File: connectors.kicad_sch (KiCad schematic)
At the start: 4 parts, among them J1 Conn_01x04_Male, J2 Conn_01x04_Male, J3 Conn_01x09_Male, J4 Conn_02x03_Odd_Even

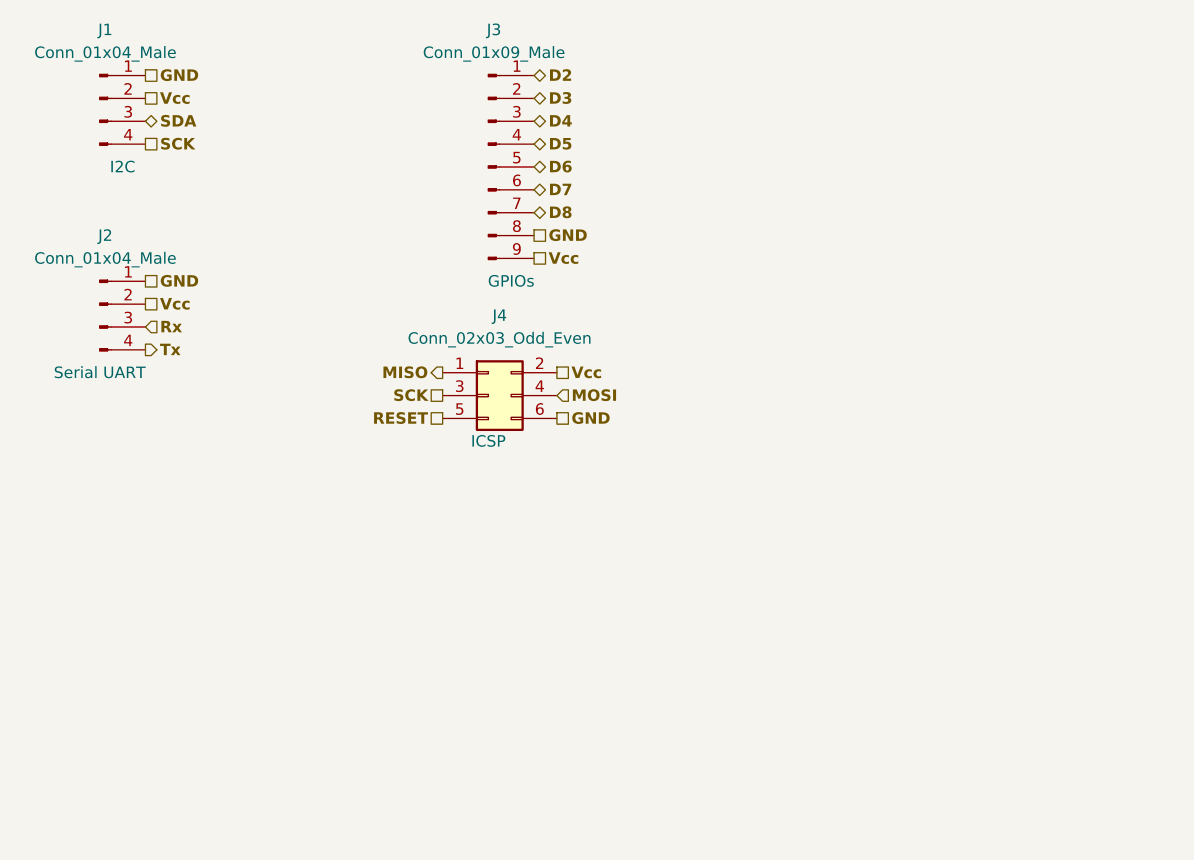
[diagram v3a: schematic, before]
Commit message: Routing GND Vcc completed
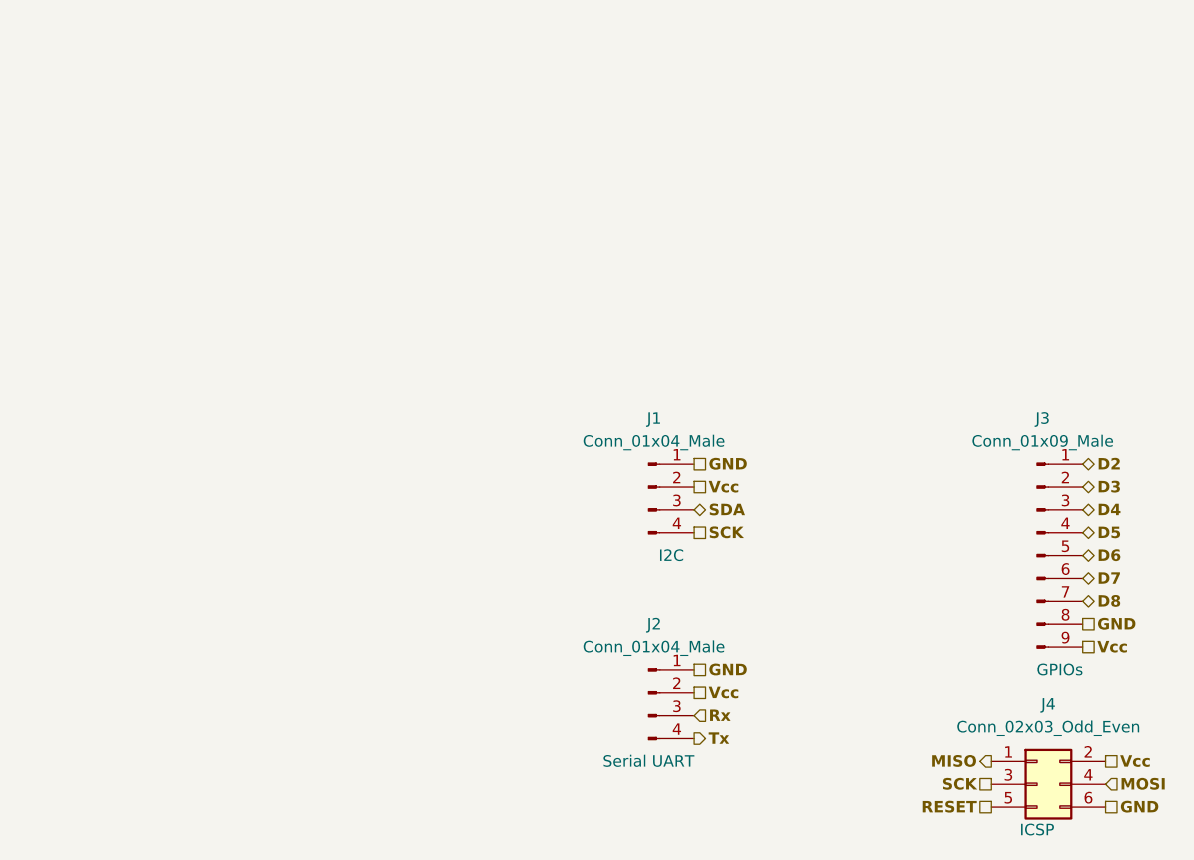
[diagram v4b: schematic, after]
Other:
- moved on the sheet: J1, J2, J3, J4
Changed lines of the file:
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@@
 (kicad_sch (version 20211123) (generator eeschema)
   (paper "A4")
-  (hierarchical_label "GND" (shape passive) (at 109.22 50.8 0)
+  (hierarchical_label "GND" (shape passive) (at 170.18 93.98 0)
     (effects (font (size 1.27 1.27) bold) (justify left))
   )
-  (hierarchical_label "D6" (shape bidirectional) (at 109.22 43.18 0)
+  (hierarchical_label "D6" (shape bidirectional) (at 170.18 86.36 0)
     (effects (font (size 1.27 1.27) bold) (justify left))
   )
-  (hierarchical_label "SCK" (shape passive) (at 66.04 40.64 0)
+  (hierarchical_label "SCK" (shape passive) (at 127 83.82 0)
     (effects (font (size 1.27 1.27) bold) (justify left))
   )
-  (hierarchical_label "D3" (shape bidirectional) (at 109.22 35.56 0)
+  (hierarchical_label "D3" (shape bidirectional) (at 170.18 78.74 0)
     (effects (font (size 1.27 1.27) bold) (justify left))
   )
-  (hierarchical_label "Rx" (shape input) (at 66.04 60.96 0)
+  (hierarchical_label "Rx" (shape input) (at 127 104.14 0)
     (effects (font (size 1.27 1.27) bold) (justify left))
   )
-  (hierarchical_label "RESET" (shape passive) (at 99.06 71.12 180)
+  (hierarchical_label "RESET" (shape passive) (at 160.02 114.3 180)
     (effects (font (size 1.27 1.27) bold) (justify right))
   )
-  (hierarchical_label "D7" (shape bidirectional) (at 109.22 45.72 0)
+  (hierarchical_label "D7" (shape bidirectional) (at 170.18 88.9 0)
     (effects (font (size 1.27 1.27) bold) (justify left))
   )
-  (hierarchical_label "Tx" (shape output) (at 66.04 63.5 0)
+  (hierarchical_label "Tx" (shape output) (at 127 106.68 0)
     (effects (font (size 1.27 1.27) bold) (justify left))
   )
-  (hierarchical_label "SCK" (shape passive) (at 99.06 68.58 180)
+  (hierarchical_label "SCK" (shape passive) (at 160.02 111.76 180)
     (effects (font (size 1.27 1.27) bold) (justify right))
   )
-  (hierarchical_label "Vcc" (shape passive) (at 66.04 58.42 0)
+  (hierarchical_label "Vcc" (shape passive) (at 127 101.6 0)
     (effects (font (size 1.27 1.27) bold) (justify left))
   )
-  (hierarchical_label "D4" (shape bidirectional) (at 109.22 38.1 0)
+  (hierarchical_label "D4" (shape bidirectional) (at 170.18 81.28 0)
     (effects (font (size 1.27 1.27) bold) (justify left))
   )
-  (hierarchical_label "D2" (shape bidirectional) (at 109.22 33.02 0)
+  (hierarchical_label "D2" (shape bidirectional) (at 170.18 76.2 0)
     (effects (font (size 1.27 1.27) bold) (justify left))
   )
-  (hierarchical_label "GND" (shape passive) (at 66.04 55.88 0)
+  (hierarchical_label "GND" (shape passive) (at 127 99.06 0)
     (effects (font (size 1.27 1.27) bold) (justify left))
   )
-  (hierarchical_label "Vcc" (shape passive) (at 66.04 35.56 0)
+  (hierarchical_label "Vcc" (shape passive) (at 127 78.74 0)
     (effects (font (size 1.27 1.27) bold) (justify left))
   )
-  (hierarchical_label "SDA" (shape bidirectional) (at 66.04 38.1 0)
+  (hierarchical_label "SDA" (shape bidirectional) (at 127 81.28 0)
     (effects (font (size 1.27 1.27) bold) (justify left))
   )
-  (hierarchical_label "GND" (shape passive) (at 66.04 33.02 0)
+  (hierarchical_label "GND" (shape passive) (at 127 76.2 0)
     (effects (font (size 1.27 1.27) bold) (justify left))
   )
-  (hierarchical_label "D8" (shape bidirectional) (at 109.22 48.26 0)
+  (hierarchical_label "D8" (shape bidirectional) (at 170.18 91.44 0)
     (effects (font (size 1.27 1.27) bold) (justify left))
   )
-  (hierarchical_label "Vcc" (shape passive) (at 109.22 53.34 0)
+  (hierarchical_label "Vcc" (shape passive) (at 170.18 96.52 0)
     (effects (font (size 1.27 1.27) bold) (justify left))
   )
-  (hierarchical_label "MOSI" (shape input) (at 111.76 68.58 0)
+  (hierarchical_label "MOSI" (shape input) (at 172.72 111.76 0)
     (effects (font (size 1.27 1.27) bold) (justify left))
   )
-  (hierarchical_label "Vcc" (shape passive) (at 111.76 66.04 0)
+  (hierarchical_label "Vcc" (shape passive) (at 172.72 109.22 0)
     (effects (font (size 1.27 1.27) bold) (justify left))
   )
-  (hierarchical_label "D5" (shape bidirectional) (at 109.22 40.64 0)
+  (hierarchical_label "D5" (shape bidirectional) (at 170.18 83.82 0)
     (effects (font (size 1.27 1.27) bold) (justify left))
   )
-  (hierarchical_label "MISO" (shape output) (at 99.06 66.04 180)
+  (hierarchical_label "MISO" (shape output) (at 160.02 109.22 180)
     (effects (font (size 1.27 1.27) bold) (justify right))
   )
-  (hierarchical_label "GND" (shape passive) (at 111.76 71.12 0)
+  (hierarchical_label "GND" (shape passive) (at 172.72 114.3 0)
     (effects (font (size 1.27 1.27) bold) (justify left))
   )
-  (symbol (lib_id "Connector:Conn_01x04_Male") (at 60.96 35.56 0) (unit 1)
+  (symbol (lib_id "Connector:Conn_01x04_Male") (at 121.92 78.74 0) (unit 1)
     (in_bom yes) (on_board yes)
-    (property "Reference" "J1" (id 0) (at 61.595 27.94 0))
-    (property "Value" "Conn_01x04_Male" (id 1) (at 61.595 30.48 0))
-    (property "Footprint" "Connector_PinHeader_2.54mm:PinHeader_1x04_P2.54mm_Vertical" (id 2) (at 60.96 35.56 0)
+    (property "Reference" "J1" (id 0) (at 122.555 71.12 0))
+    (property "Value" "Conn_01x04_Male" (id 1) (at 122.555 73.66 0))
+    (property "Footprint" "Connector_PinHeader_2.54mm:PinHeader_1x04_P2.54mm_Vertical" (id 2) (at 121.92 78.74 0)
       (effects (font (size 1.27 1.27)) hide)
     )
-    (property "Datasheet" "~" (id 3) (at 60.96 35.56 0)
+    (property "Datasheet" "~" (id 3) (at 121.92 78.74 0)
       (effects (font (size 1.27 1.27)) hide)
     )
-    (property "Purpose" "I2C" (id 4) (at 63.5 43.18 0))
+    (property "Purpose" "I2C" (id 4) (at 124.46 86.36 0))
     (pin "1")
     (pin "2")
@@
     (pin "4")
   )
-  (symbol (lib_id "Connector:Conn_01x09_Male") (at 104.14 43.18 0) (unit 1)
+  (symbol (lib_id "Connector:Conn_01x09_Male") (at 165.1 86.36 0) (unit 1)
     (in_bom yes) (on_board yes)
-    (property "Reference" "J3" (id 0) (at 104.775 27.94 0))
-    (property "Value" "Conn_01x09_Male" (id 1) (at 104.775 30.48 0))
-    (property "Footprint" "Connector_PinHeader_2.54mm:PinHeader_1x09_P2.54mm_Vertical" (id 2) (at 104.14 43.18 0)
+    (property "Reference" "J3" (id 0) (at 165.735 71.12 0))
+    (property "Value" "Conn_01x09_Male" (id 1) (at 165.735 73.66 0))
+    (property "Footprint" "Connector_PinHeader_2.54mm:PinHeader_1x09_P2.54mm_Vertical" (id 2) (at 165.1 86.36 0)
       (effects (font (size 1.27 1.27)) hide)
     )
-    (property "Datasheet" "~" (id 3) (at 104.14 43.18 0)
+    (property "Datasheet" "~" (id 3) (at 165.1 86.36 0)
       (effects (font (size 1.27 1.27)) hide)
     )
-    (property "Purpose" "GPIOs" (id 4) (at 106.68 55.88 0))
+    (property "Purpose" "GPIOs" (id 4) (at 167.64 99.06 0))
     (pin "1")
     (pin "2")
@@
     (pin "9")
   )
-  (symbol (lib_id "Connector:Conn_01x04_Male") (at 60.96 58.42 0) (unit 1)
+  (symbol (lib_id "Connector:Conn_01x04_Male") (at 121.92 101.6 0) (unit 1)
     (in_bom yes) (on_board yes)
-    (property "Reference" "J2" (id 0) (at 61.595 50.8 0))
-    (property "Value" "Conn_01x04_Male" (id 1) (at 61.595 53.34 0))
-    (property "Footprint" "Connector_PinHeader_2.54mm:PinHeader_1x04_P2.54mm_Vertical" (id 2) (at 60.96 58.42 0)
+    (property "Reference" "J2" (id 0) (at 122.555 93.98 0))
+    (property "Value" "Conn_01x04_Male" (id 1) (at 122.555 96.52 0))
+    (property "Footprint" "Connector_PinHeader_2.54mm:PinHeader_1x04_P2.54mm_Vertical" (id 2) (at 121.92 101.6 0)
       (effects (font (size 1.27 1.27)) hide)
     )
-    (property "Datasheet" "~" (id 3) (at 60.96 58.42 0)
+    (property "Datasheet" "~" (id 3) (at 121.92 101.6 0)
       (effects (font (size 1.27 1.27)) hide)
     )
-    (property "Purpose" "Serial UART" (id 4) (at 60.96 66.04 0))
+    (property "Purpose" "Serial UART" (id 4) (at 121.92 109.22 0))
     (pin "1")
     (pin "2")
@@
     (pin "4")
   )
-  (symbol (lib_id "Connector_Generic:Conn_02x03_Odd_Even") (at 104.14 68.58 0) (unit 1)
+  (symbol (lib_id "Connector_Generic:Conn_02x03_Odd_Even") (at 165.1 111.76 0) (unit 1)
     (in_bom yes) (on_board yes)
-    (property "Reference" "J4" (id 0) (at 105.41 59.69 0))
-    (property "Value" "Conn_02x03_Odd_Even" (id 1) (at 105.41 62.23 0))
-    (property "Footprint" "Connector_PinHeader_2.54mm:PinHeader_2x03_P2.54mm_Vertical" (id 2) (at 104.14 68.58 0)
+    (property "Reference" "J4" (id 0) (at 166.37 102.87 0))
+    (property "Value" "Conn_02x03_Odd_Even" (id 1) (at 166.37 105.41 0))
+    (property "Footprint" "Connector_PinHeader_2.54mm:PinHeader_2x03_P2.54mm_Vertical" (id 2) (at 165.1 111.76 0)
       (effects (font (size 1.27 1.27)) hide)
     )
-    (property "Datasheet" "~" (id 3) (at 104.14 68.58 0)
+    (property "Datasheet" "~" (id 3) (at 165.1 111.76 0)
       (effects (font (size 1.27 1.27)) hide)
     )
-    (property "Field4" "ICSP" (id 4) (at 104.14 73.66 0))
+    (property "Field4" "ICSP" (id 4) (at 165.1 116.84 0))
     (pin "1")
     (pin "2")

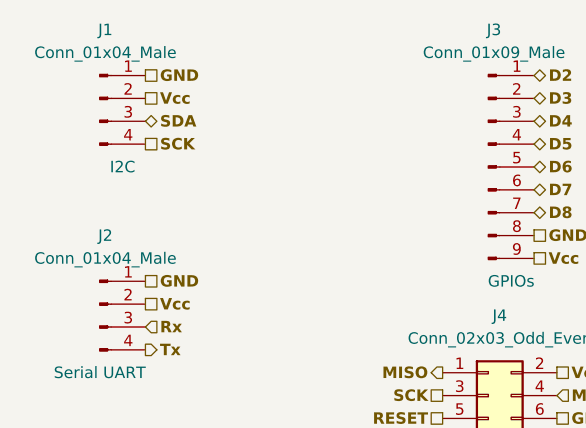
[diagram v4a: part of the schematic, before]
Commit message: sch modification - correction SCL
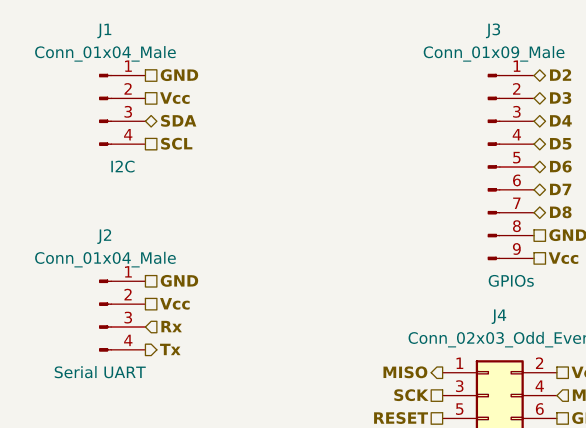
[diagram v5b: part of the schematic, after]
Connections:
- net SCK: no longer J1.4 (Pin_4)
- new net SCL: J1.4 (Pin_4)
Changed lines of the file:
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@@
     (effects (font (size 1.27 1.27) bold) (justify left))
   )
-  (hierarchical_label "SCK" (shape passive) (at 127 83.82 0)
+  (hierarchical_label "SCL" (shape passive) (at 127 83.82 0)
     (effects (font (size 1.27 1.27) bold) (justify left))
   )
